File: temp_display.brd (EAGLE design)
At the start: 101.6 x 76.2 mm, 71 parts, among them IC2 ATMEGA168PROUND, Q1 2N2907, Q2 FQN1N50C, T1 BC547

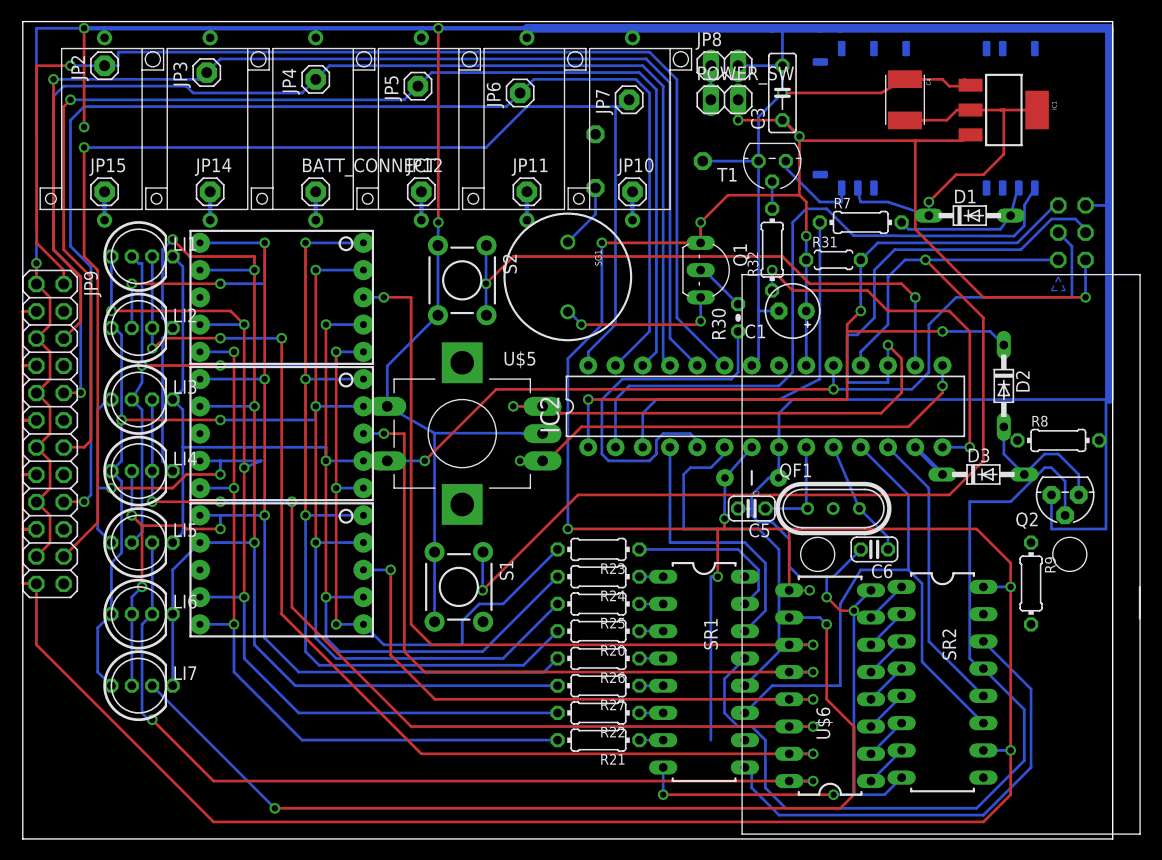
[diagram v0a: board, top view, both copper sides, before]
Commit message: Fixed some shorts. Now need to align indicators and code (wrong LEDs light up)
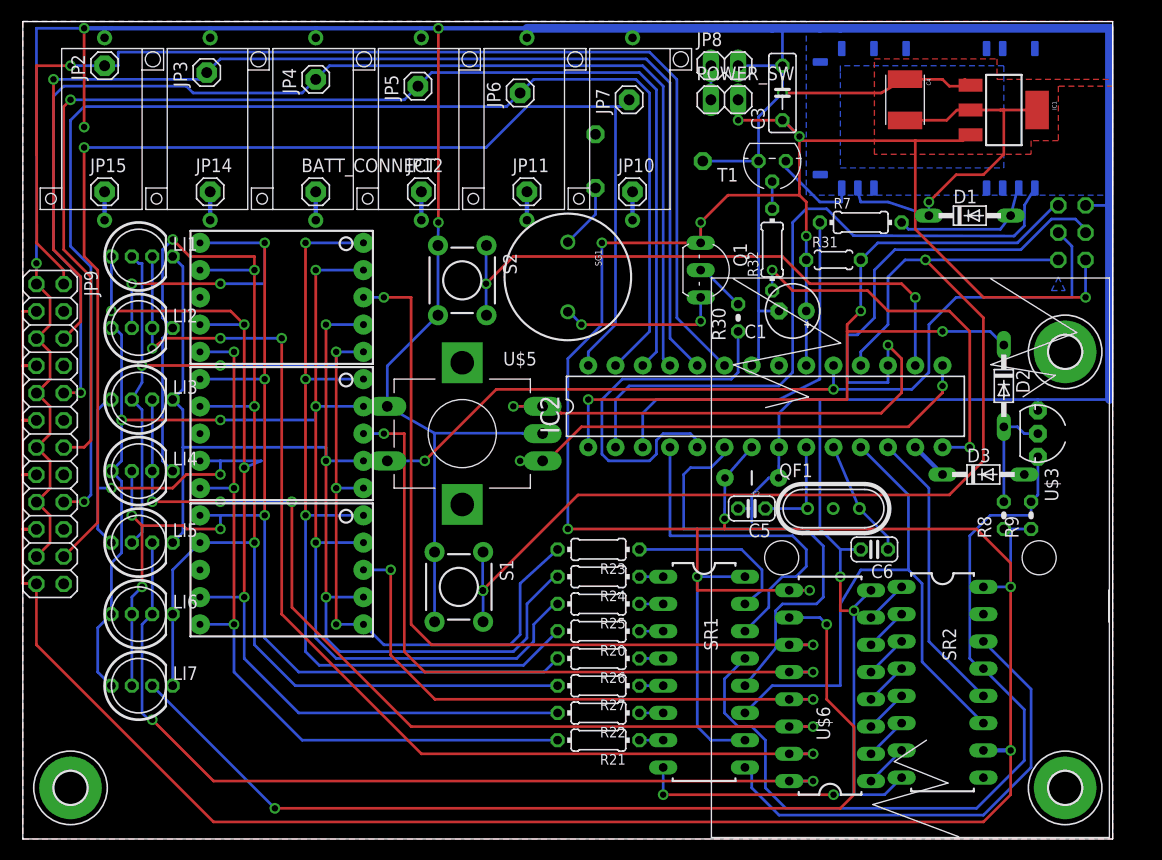
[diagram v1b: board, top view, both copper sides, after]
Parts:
- removed Q2: FQN1N50C, adafruit:TO92
- added H1, H2, H3: MOUNT-PAD-ROUND3.0, holes:3,0-PAD
- added U$3: 2N7000, kirill:TO-92
- R8, R9: device resistor:0204/7 -> resistor:0204V
- moved R8 8.64 mm to (91.4, 29.8), turned to 90 degrees
- moved R9 6.35 mm to (94.0, 29.8), turned to 90 degrees
- moved U$2 2.88 mm to (82.2, 28.9)
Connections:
- removed net +5: C1.+, C2.2, C3.1, IC1.3, IC2.20, IC2.7, JP1.2, JP9.11, JP9.15, JP9.19, JP9.23, JP9.3, JP9.7, POWER_SW.2, Q1.E, R31.1, SR2.10, SR2.16, U$6.9
- new net N$16: JP8.1, POWER_SW.1
- net +5V: now also C1.+, C2.2, C3.1, IC1.3, IC2.20, IC2.7, JP1.2, JP9.11, JP9.15, JP9.19, JP9.23, JP9.3, JP9.7, POWER_SW.2, Q1.E, R31.1, SR2.10, SR2.16, U$6.9; no longer JP8.1, POWER_SW.1
- net GND: now also U$3.1; no longer Q2.3
- net N$14: now also U$3.2; no longer Q2.1
- net OE: now also U$3.3; no longer Q2.2
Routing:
- net +5V: track 3.17 -> 399.6 mm, vias 0 -> 12
- net +5: track 380.3 -> 0.00 mm, vias 12 -> 0
- net GND: track 471.4 -> 456.3 mm
- net STCP1: track 34.0 -> 41.7 mm
- net DS: track 25.7 -> 32.2 mm
- net OE: track 82.3 -> 77.4 mm
- net N$16: track 0.00 -> 3.17 mm
- net N$27: track 102.1 -> 105.0 mm, vias 2 -> 3
- net SEG_D: track 107.5 -> 109.4 mm
- net N$14: track 13.8 -> 12.3 mm
- net SEG_E: track 104.6 -> 106.0 mm
- net SEG_C: track 128.6 -> 129.5 mm
- net N$26: track 15.6 -> 16.2 mm
- added copper zone on layer 1, net GND
- added copper zone on layer 16, net GND
- added copper zone on layer 16, net N$17
